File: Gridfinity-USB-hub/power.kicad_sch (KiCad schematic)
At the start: 0 parts

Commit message: V2 complete, ready for review and polish
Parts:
- added C32, C33: 0.1u, Capacitor_SMD:C_0402_1005Metric, symbol Device:C_Small
- added J11, J12: Conn_01x02, Connector_PinSocket_2.54mm:PinSocket_1x02_P2.54mm_Vertical, symbol Connector_Generic:Conn_01x02
- added JP5: Jumper_2_Small_Bridged, Jumper:SolderJumper-2_P1.3mm_Bridged2Bar_RoundedPad1.0x1.5mm, symbol Jumper:Jumper_2_Small_Bridged
- added TH1: 6V/2A, Resistor_SMD:R_0603_1608Metric, symbol Device:Thermistor_PTC
- added U5: AP2112K-3.3, Package_TO_SOT_SMD:SOT-23-5, symbol PartsBox:AP2112K-3.3TRG1
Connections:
- net +3V3: now also JP5.2 (B)
- net VBUS: now also C33.1, TH1.1, U5.1 (VIN), U5.3 (EN)
- new net: C32.1, J12.1 (Pin_1), JP5.1 (A), U5.5 (VOUT)
- new net +5V: J11.1 (Pin_1), TH1.2
- new net GND: C32.2, C33.2, J11.2 (Pin_2), J12.2 (Pin_2), U5.2 (GND)

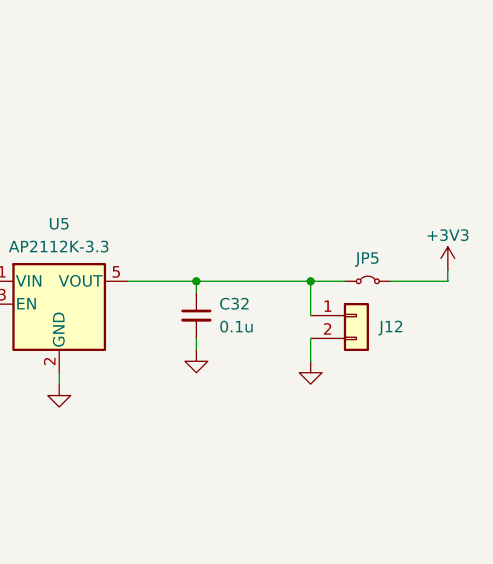
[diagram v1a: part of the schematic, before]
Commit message: Add 3x channels of spare LEDs for general breadboard use, add silkscreen.  Ordered this version
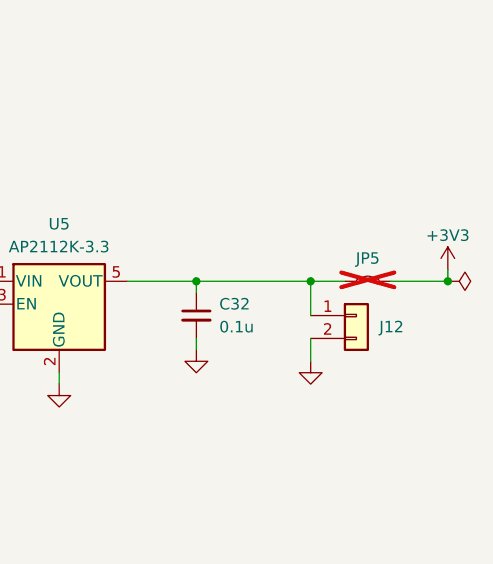
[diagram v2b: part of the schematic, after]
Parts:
- C32, C33: JLCPCB Part No. (none) -> C77020; MPN (none) -> GRM155R71H104KE14D
- J11, J12: FT Rotation Offset (none) -> 90; JLCPCB Part No. (none) -> C492401; MPN (none) -> PZ254V-11-02P
- JP5: now not fitted
- U5: FT Rotation Offset 90 -> (none); JLCPCB Part No. C51118 -> C23380830
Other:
- company: (none) -> SK Electronics Consulting LLC
- title: (none) -> USB 2.0 Hub for Gridifinity
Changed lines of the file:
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@@
 	(generator_version "9.0")
 	(paper "A4")
+	(title_block
+		(title "USB 2.0 Hub for Gridifinity")
+		(date "2026-02-16")
+		(rev "2")
+		(company "SK Electronics Consulting LLC")
+	)
 	(junction
 		(at 60.96 69.85)
@@
 	(junction
 		(at 125.73 88.9)
+		(diameter 0)
+		(color 0 0 0 0)
+	)
+	(junction
+		(at 153.67 88.9)
 		(diameter 0)
 		(color 0 0 0 0)
@@
 			)
 		)
-		(property "FT Rotation Offset" "90"
+		(property "FT Rotation Offset" ""
 			(at 110.49 91.44 0)
 			(effects
@@
 			)
 		)
-		(property "JLCPCB Part No." "C51118"
+		(property "JLCPCB Part No." "C23380830"
 			(at 110.49 91.44 0)
 			(effects
@@
 		(in_bom yes)
 		(on_board yes)
-		(dnp no)
+		(dnp yes)
 		(property "Reference" "JP5"
 			(at 144.78 86.36 0)
@@
 			)
 		)
-		(property "JLCPCB Part No." ""
+		(property "JLCPCB Part No." "C77020"
 			(at 93.98 92.71 0)
 			(effects
@@
 		)
 		(property "KLC_S4.2_VREGOUT" ""
+			(at 93.98 92.71 0)
+			(effects
+				(font
+					(size 1.27 1.27)
+				)
+				(hide yes)
+			)
+		)
+		(property "MPN" "GRM155R71H104KE14D"
 			(at 93.98 92.71 0)
 			(effects
@@
 	)
 	(symbol
+		(lib_id "power:PWR_FLAG")
+		(at 153.67 88.9 270)
+		(unit 1)
+		(exclude_from_sim no)
+		(in_bom yes)
+		(on_board yes)
+		(dnp no)
+		(fields_autoplaced yes)
+		(property "Reference" "#FLG08"
+			(at 155.575 88.9 0)
+			(effects
+				(font
+					(size 1.27 1.27)
+				)
+				(hide yes)
+			)
+		)
+		(property "Value" "PWR_FLAG"
+			(at 157.48 88.8999 90)
+			(effects
+				(font
+					(size 1.27 1.27)
+				)
+				(justify left)
+				(hide yes)
+			)
+		)
+		(property "Footprint" ""
+			(at 153.67 88.9 0)
+			(effects
+				(font
+					(size 1.27 1.27)
+				)
+				(hide yes)
+			)
+		)
+		(property "Datasheet" "~"
+			(at 153.67 88.9 0)
+			(effects
+				(font
+					(size 1.27 1.27)
+				)
+				(hide yes)
+			)
+		)
+		(property "Description" "Special symbol for telling ERC where power comes from"
+			(at 153.67 88.9 0)
+			(effects
+				(font
+					(size 1.27 1.27)
+				)
+				(hide yes)
+			)
+		)
+		(pin "1"
+		)
+		(instances
+			(project ""
+				(path "/74fafa03-a255-46ac-b2a3-3905ac0a0772/0b8e50e6-cc3e-49b7-8502-b97225662dee"
+					(reference "#FLG08")
+					(unit 1)
+				)
+			)
+		)
+	)
+	(symbol
 		(lib_id "power:+3V3")
 		(at 153.67 87.63 0)
@@
 			)
 		)
-		(property "JLCPCB Part No." ""
+		(property "JLCPCB Part No." "C77020"
 			(at 125.73 92.71 0)
 			(effects
@@
 		)
 		(property "KLC_S4.2_VREGOUT" ""
+			(at 125.73 92.71 0)
+			(effects
+				(font
+					(size 1.27 1.27)
+				)
+				(hide yes)
+			)
+		)
+		(property "MPN" "GRM155R71H104KE14D"
 			(at 125.73 92.71 0)
 			(effects
@@
 			)
 		)
+		(property "FT Rotation Offset" "90"
+			(at 69.85 121.92 0)
+			(effects
+				(font
+					(size 1.27 1.27)
+				)
+				(hide yes)
+			)
+		)
+		(property "JLCPCB Part No." "C492401"
+			(at 69.85 121.92 0)
+			(effects
+				(font
+					(size 1.27 1.27)
+				)
+				(hide yes)
+			)
+		)
+		(property "MPN" "PZ254V-11-02P"
+			(at 69.85 121.92 0)
+			(effects
+				(font
+					(size 1.27 1.27)
+				)
+				(hide yes)
+			)
+		)
 		(pin "1"
 		)
@@
 			(at 143.51 92.71 0)
 			(effects
+				(font
+					(size 1.27 1.27)
+				)
+				(hide yes)
+			)
+		)
+		(property "FT Rotation Offset" "90"
+			(at 143.51 92.71 0)
+			(effects
+				(font
+					(size 1.27 1.27)
+				)
+				(hide yes)
+			)
+		)
+		(property "JLCPCB Part No." "C492401"
+			(at 143.51 92.71 0)
+			(effects
+				(font
+					(size 1.27 1.27)
+				)
+				(hide yes)
+			)
+		)
+		(property "MPN" "PZ254V-11-02P"
+			(at 143.51 92.71 0)
+			(effects
